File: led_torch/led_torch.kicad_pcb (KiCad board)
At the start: 2 copper layers, 64 x 26.5 mm, 4 parts, among them SW1 SW_DPDT_x2

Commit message: logos
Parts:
- added G***: LOGO, JPI_LOGOS:jpi_logo_text_10mm_silkscreen, B.Cu at (165.8, 127.0)

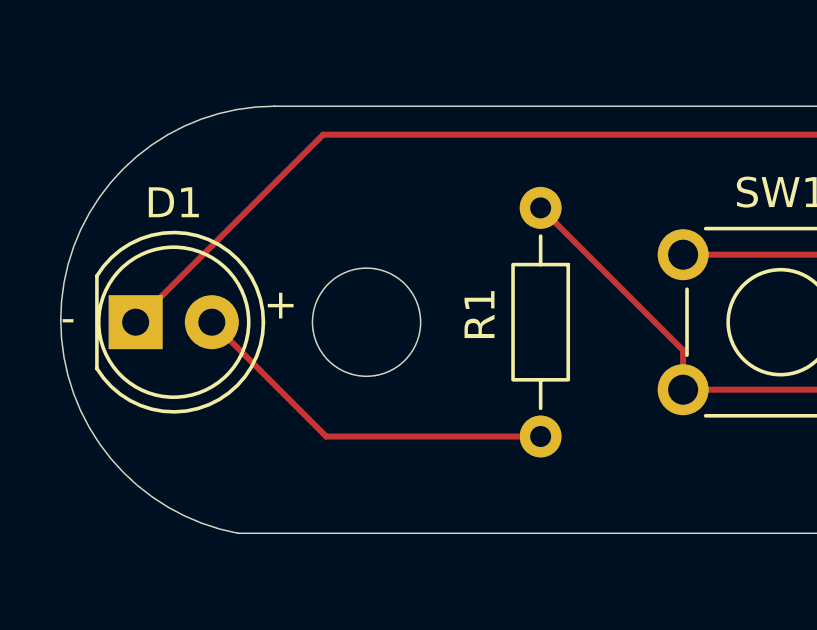
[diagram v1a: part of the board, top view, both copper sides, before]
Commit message: logos corrected
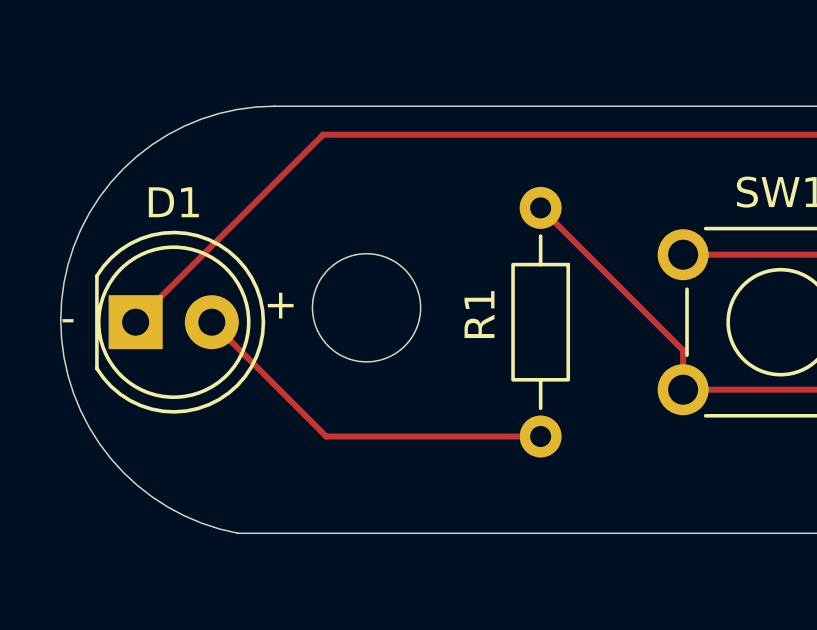
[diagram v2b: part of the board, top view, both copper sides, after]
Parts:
- removed the G*** at (165.8, 127.0)
- added G***: LOGO, JPI_LOGOS:jpi_test, B.Cu at (166.4, 127.0)
- added G***: LOGO, JPI_LOGOS:jpi_logo_10mm_silkscreen, B.Cu at (181.6, 121.9)
- added G***: LOGO, JPI_LOGOS:jpi_logo_only_10mm_silkscreen, B.Cu at (165.4, 116.8)
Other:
- outline, holes or cut-outs redrawn
